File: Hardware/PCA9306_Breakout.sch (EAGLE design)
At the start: 15 parts

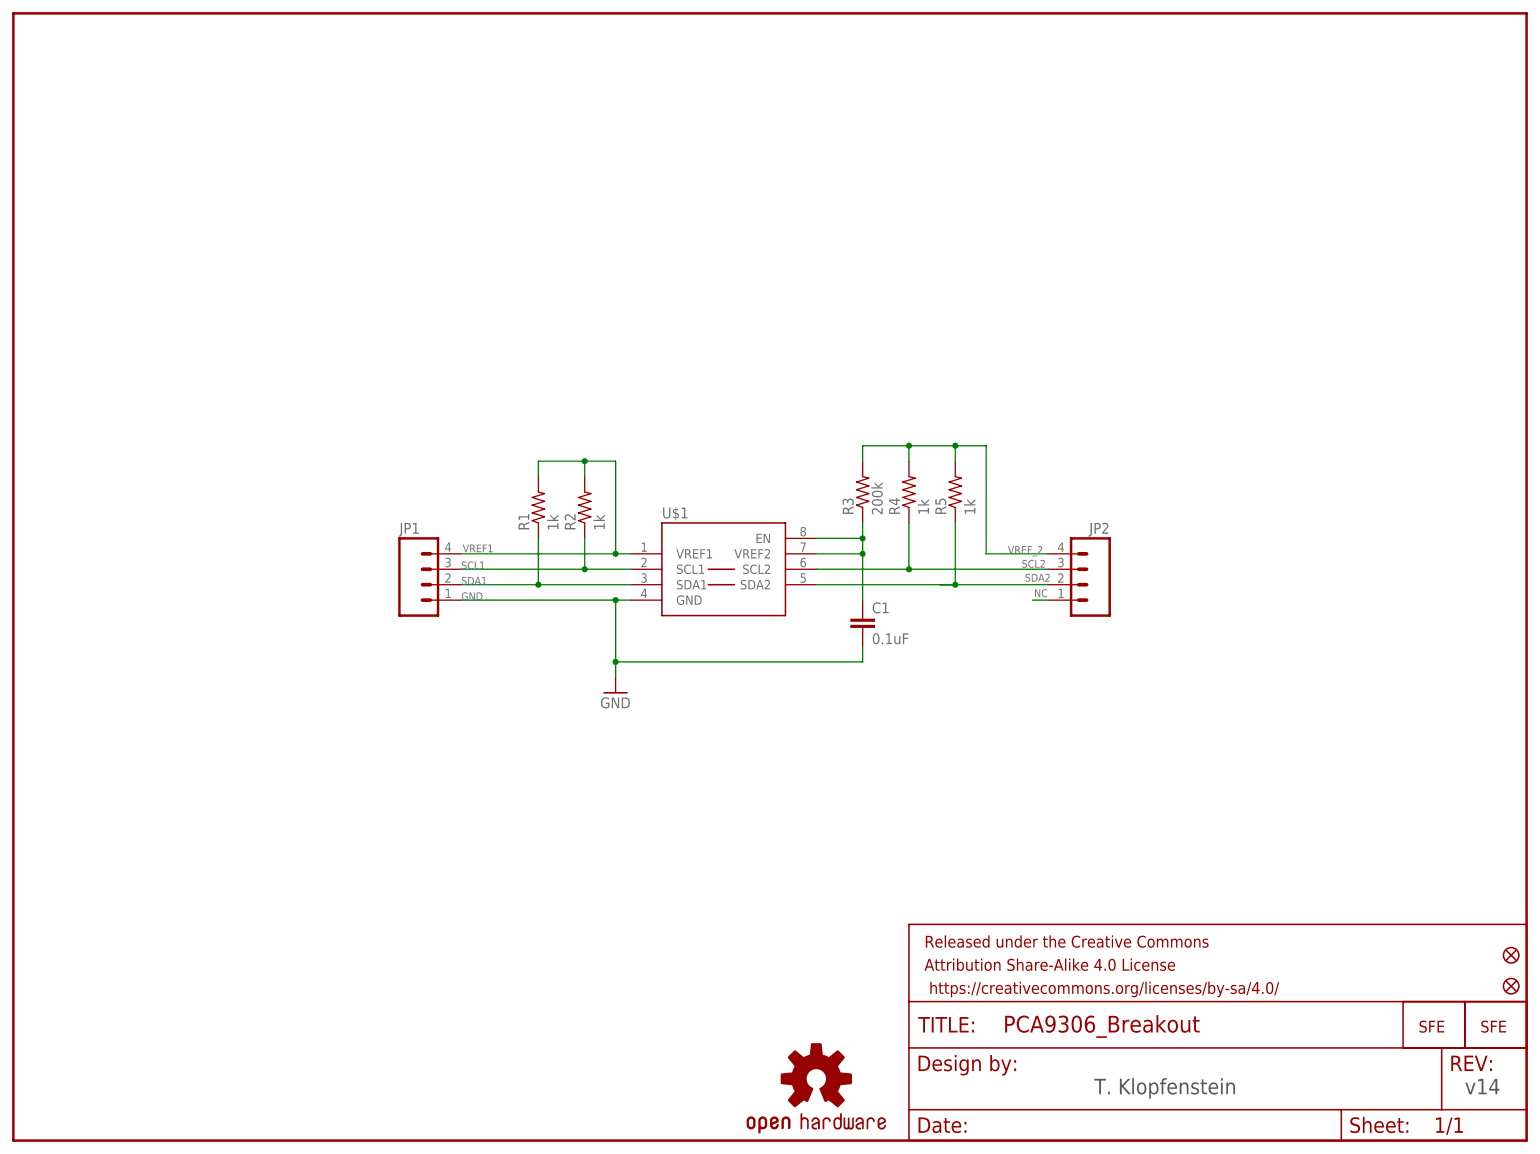
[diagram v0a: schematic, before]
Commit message: Adds slik lables, adds jumper for enable pin, increases size by 10 mils in both x and y direction, updates PCA9306 to new package
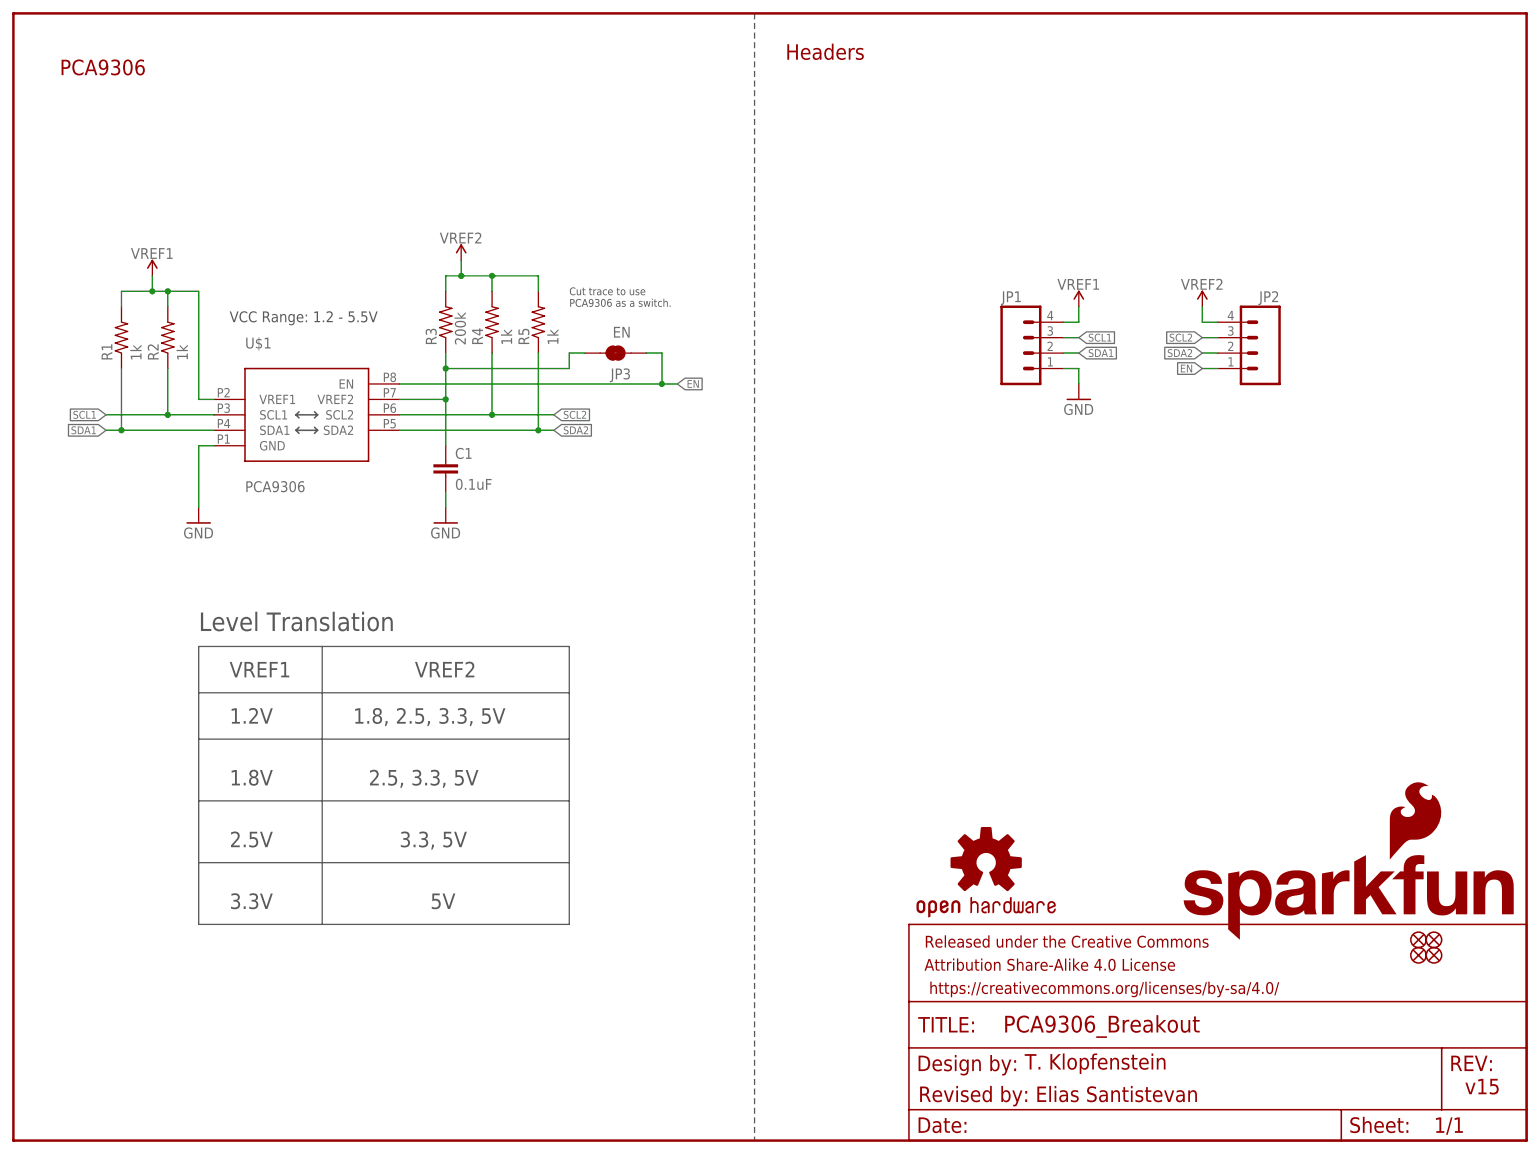
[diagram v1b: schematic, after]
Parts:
- removed JP4: LOGO-SFESK, SparkFun:LOGO-SFESK
- removed JP7, JP8: FIDUCIAL1X2.5, abes:FIDUCIAL1X2.5
- added FD1, FD2, FD3, FD4: FIDUCIALUFIDUCIAL, SparkFun-Aesthetics:FIDUCIALUFIDUCIAL
- added LOGO2: SFE_LOGO_FLAME.1_INCH, SparkFun-Aesthetics:SFE_LOGO_FLAME.1_INCH
- added LOGO3: SFE_LOGO_NAME.1_INCH, SparkFun-Aesthetics:SFE_LOGO_NAME.1_INCH
- C1: device SparkFun:CAP0603-CAP -> SparkFun-Capacitors:0.1UF-0603-25V-(+80/-20%)
- JP1, JP2: device SparkFun:M04PTH -> SparkFun-Connectors:CONN_041X04_NO_SILK
- JP3: value LOGO-SFESK -> EN; device SparkFun:LOGO-SFESK -> SparkFun-Jumpers:JUMPER-SMT_2_NC_TRACE_SILK
- R1, R2, R4, R5: device SparkFun:RESISTOR0603-RES -> SparkFun-Resistors:1KOHM-0603-1/10W-1%
- R3: device SparkFun:RESISTOR0603-RES -> SparkFun-Resistors:200KOHM-0603-1/10W-1%
- U$1: value (none) -> PCA9306; device SparkFun-DigitalIC:PCA9306 -> SparkFun-IC-Comms:PCA9306VSSOP_8PIN
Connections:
- removed net NC: JP2.1
- removed net VREF_2: JP2.4, R3.2, R4.2, R5.2
- new net EN: JP2.1, JP3.1, U$1.EN
- new net VREF2_IN: C1.1, JP3.2, R3.1, U$1.VREF2
- net VREF2: now also JP2.4, R3.2, R4.2, R5.2; no longer C1.1, R3.1, U$1.EN, U$1.VREF2
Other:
- note added: "1.2V"
- note added: "1.8, 2.5, 3.3, 5V"
- note added: "1.8V"
- note added: "2.5, 3.3, 5V"
- note added: "2.5V"
- note added: "3.3, 5V"
- note added: "3.3V"
- note added: "5V"
- note added: "Cut trace to use PCA9306 as a switch."
- note added: "Headers"
- note added: "Level Translation"
- note added: "PCA9306"
- note added: "Revised by: Elias Santistevan"
- note added: "VCC Range: 1.2 - 5.5V"
- note added: "VREF1"
- note added: "VREF2"
- note added: "v15"
- note removed: "v14"
- moved on the sheet: C1, R1, R2, R3, R4, R5

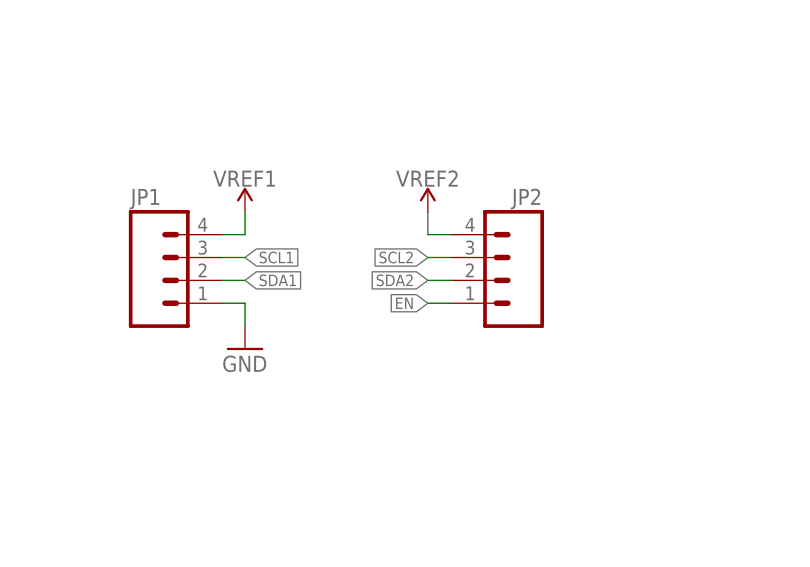
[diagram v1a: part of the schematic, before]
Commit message: Adds an additional PTH header for GND on VREF2 side
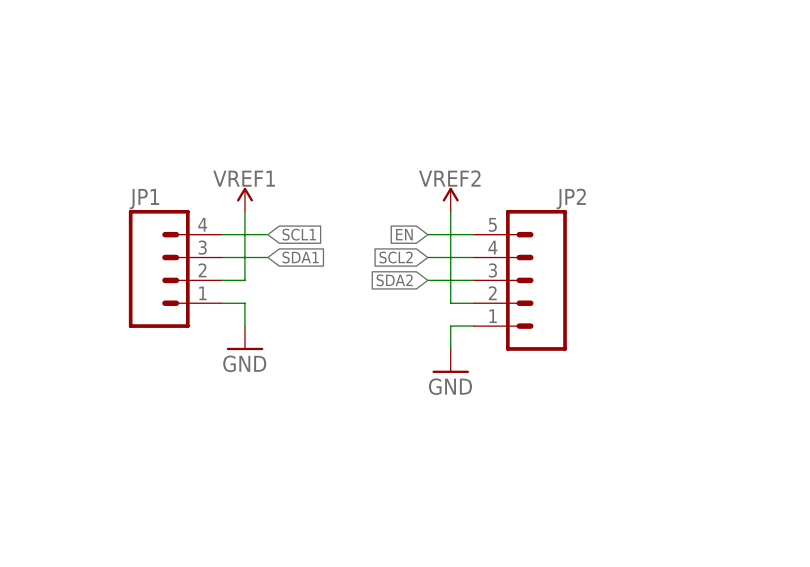
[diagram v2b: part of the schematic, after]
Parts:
- JP2: device SparkFun-Connectors:CONN_041X04_NO_SILK -> SparkFun-Connectors:CONN_05NO_SILK
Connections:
- net EN: now also JP2.5; no longer JP2.1
- net GND: now also JP2.1
- net SCL1: now also JP1.4; no longer JP1.3
- net SCL2: now also JP2.4; no longer JP2.3
- net SDA1: now also JP1.3; no longer JP1.2
- net SDA2: now also JP2.3; no longer JP2.2
- net VREF1: now also JP1.2; no longer JP1.4
- net VREF2: now also JP2.2; no longer JP2.4
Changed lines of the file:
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@@
 <part name="GND1" library="SparkFun-PowerSymbols" deviceset="GND" device=""/>
 <part name="JP1" library="SparkFun-Connectors" deviceset="CONN_04" device="1X04_NO_SILK"/>
-<part name="JP2" library="SparkFun-Connectors" deviceset="CONN_04" device="1X04_NO_SILK"/>
+<part name="JP2" library="SparkFun-Connectors" deviceset="CONN_05" device="NO_SILK"/>
 <part name="LOGO1" library="SparkFun-Aesthetics" deviceset="OSHW-LOGO" device="S"/>
 <part name="SUPPLY1" library="SparkFun-PowerSymbols" deviceset="VREF1" device=""/>
@@
 <part name="FD4" library="SparkFun-Aesthetics" deviceset="FIDUCIAL" device="UFIDUCIAL"/>
 <part name="LOGO3" library="SparkFun-Aesthetics" deviceset="SFE_LOGO_NAME" device=".1_INCH"/>
+<part name="GND4" library="SparkFun-PowerSymbols" deviceset="GND" device=""/>
 </parts>
 <sheets>
@@
 <attribute name="NAME" x="162.56" y="137.922" size="1.778" layer="95"/>
 </instance>
-<instance part="JP2" gate="J1" x="203.2" y="129.54" smashed="yes" rot="MR0">
-<attribute name="VALUE" x="208.28" y="121.92" size="1.778" layer="96" rot="MR0"/>
-<attribute name="NAME" x="208.28" y="137.922" size="1.778" layer="95" rot="MR0"/>
+<instance part="JP2" gate="G$1" x="208.28" y="129.54" smashed="yes" rot="MR0">
+<attribute name="VALUE" x="213.36" y="121.92" size="1.778" layer="96" rot="MR0"/>
+<attribute name="NAME" x="213.36" y="137.922" size="1.778" layer="95" rot="MR0"/>
 </instance>
 <instance part="LOGO1" gate="G$1" x="160.02" y="45.72" smashed="yes"/>
@@
 <attribute name="VALUE" x="175.26" y="139.954" size="1.778" layer="96" align="bottom-center"/>
 </instance>
-<instance part="SUPPLY4" gate="G$1" x="195.58" y="137.16" smashed="yes">
-<attribute name="VALUE" x="195.58" y="139.954" size="1.778" layer="96" align="bottom-center"/>
+<instance part="SUPPLY4" gate="G$1" x="198.12" y="137.16" smashed="yes">
+<attribute name="VALUE" x="198.12" y="139.954" size="1.778" layer="96" align="bottom-center"/>
 </instance>
 <instance part="JP3" gate="G$1" x="99.06" y="129.54" smashed="yes" rot="R180">
@@
 <instance part="FD4" gate="G$1" x="233.68" y="30.48" smashed="yes"/>
 <instance part="LOGO3" gate="G$1" x="190.5" y="33.02" smashed="yes"/>
+<instance part="GND4" gate="1" x="198.12" y="119.38" smashed="yes">
+<attribute name="VALUE" x="195.58" y="116.84" size="1.778" layer="96"/>
+</instance>
 </instances>
 <busses>
@@
 </segment>
 <segment>
-<pinref part="JP1" gate="J1" pin="3"/>
-<wire x1="172.72" y1="132.08" x2="175.26" y2="132.08" width="0.1524" layer="91"/>
-<label x="175.26" y="132.08" size="1.27" layer="95" font="vector" xref="yes"/>
+<pinref part="JP1" gate="J1" pin="4"/>
+<wire x1="172.72" y1="134.62" x2="177.8" y2="134.62" width="0.1524" layer="91"/>
+<label x="177.8" y="134.62" size="1.27" layer="95" xref="yes"/>
 </segment>
 </net>
@@
 </segment>
 <segment>
-<pinref part="JP1" gate="J1" pin="2"/>
-<wire x1="172.72" y1="129.54" x2="175.26" y2="129.54" width="0.1524" layer="91"/>
-<label x="175.26" y="129.54" size="1.27" layer="95" font="vector" xref="yes"/>
+<pinref part="JP1" gate="J1" pin="3"/>
+<wire x1="172.72" y1="132.08" x2="177.8" y2="132.08" width="0.1524" layer="91"/>
+<label x="177.8" y="132.08" size="1.27" layer="95" xref="yes"/>
 </segment>
 </net>
@@
 <pinref part="GND3" gate="1" pin="GND"/>
 <wire x1="175.26" y1="127" x2="175.26" y2="124.46" width="0.1524" layer="91"/>
+</segment>
+<segment>
+<pinref part="JP2" gate="G$1" pin="1"/>
+<wire x1="200.66" y1="124.46" x2="198.12" y2="124.46" width="0.1524" layer="91"/>
+<pinref part="GND4" gate="1" pin="GND"/>
+<wire x1="198.12" y1="121.92" x2="198.12" y2="124.46" width="0.1524" layer="91"/>
 </segment>
 </net>
@@
 </segment>
 <segment>
-<pinref part="JP2" gate="J1" pin="4"/>
-<wire x1="198.12" y1="134.62" x2="195.58" y2="134.62" width="0.1524" layer="91"/>
-<wire x1="195.58" y1="134.62" x2="195.58" y2="137.16" width="0.1524" layer="91"/>
+<pinref part="JP2" gate="G$1" pin="2"/>
+<wire x1="200.66" y1="127" x2="198.12" y2="127" width="0.1524" layer="91"/>
 <pinref part="SUPPLY4" gate="G$1" pin="VREF2"/>
+<wire x1="198.12" y1="127" x2="198.12" y2="137.16" width="0.1524" layer="91"/>
 </segment>
 </net>
@@
 </segment>
 <segment>
-<pinref part="JP2" gate="J1" pin="3"/>
-<wire x1="198.12" y1="132.08" x2="195.58" y2="132.08" width="0.1524" layer="91"/>
-<label x="195.58" y="132.08" size="1.27" layer="95" font="vector" rot="R180" xref="yes"/>
+<pinref part="JP2" gate="G$1" pin="4"/>
+<wire x1="200.66" y1="132.08" x2="195.58" y2="132.08" width="0.1524" layer="91"/>
+<label x="195.58" y="132.08" size="1.27" layer="95" rot="R180" xref="yes"/>
 </segment>
 </net>
@@
 </segment>
 <segment>
-<pinref part="JP2" gate="J1" pin="2"/>
-<wire x1="198.12" y1="129.54" x2="195.58" y2="129.54" width="0.1524" layer="91"/>
-<label x="195.58" y="129.54" size="1.27" layer="95" font="vector" rot="R180" xref="yes"/>
+<pinref part="JP2" gate="G$1" pin="3"/>
+<wire x1="200.66" y1="129.54" x2="195.58" y2="129.54" width="0.1524" layer="91"/>
+<label x="195.58" y="129.54" size="1.27" layer="95" rot="R180" xref="yes"/>
 </segment>
 </net>
@@
 </segment>
 <segment>
-<pinref part="JP1" gate="J1" pin="4"/>
-<wire x1="172.72" y1="134.62" x2="175.26" y2="134.62" width="0.1524" layer="91"/>
-<wire x1="175.26" y1="134.62" x2="175.26" y2="137.16" width="0.1524" layer="91"/>
+<pinref part="JP1" gate="J1" pin="2"/>
+<wire x1="172.72" y1="129.54" x2="175.26" y2="129.54" width="0.1524" layer="91"/>
 <pinref part="SUPPLY3" gate="G$1" pin="VREF1"/>
+<wire x1="175.26" y1="129.54" x2="175.26" y2="137.16" width="0.1524" layer="91"/>
 </segment>
 </net>
@@
 </segment>
 <segment>
-<pinref part="JP2" gate="J1" pin="1"/>
-<wire x1="198.12" y1="127" x2="195.58" y2="127" width="0.1524" layer="91"/>
-<label x="195.58" y="127" size="1.27" layer="95" font="vector" rot="R180" xref="yes"/>
-</segment>
-</net>
+<pinref part="JP2" gate="G$1" pin="5"/>
+<label x="195.58" y="134.62" size="1.27" layer="95" rot="R180" xref="yes"/>
+<wire x1="200.66" y1="134.62" x2="195.58" y2="134.62" width="0.1524" layer="91"/>
+</segment>
+</net>

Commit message: Moves passives to lower half of board, resulting in full retrace of board....
*Adds HIGH/LOW silk to board
*Adds triple jumper to correctly add enable feature
*Changes 0.1uF capacitor to 100pF capacitor
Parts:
- removed JP3: EN, SparkFun-Jumpers:JUMPER-SMT_2_NC_TRACE_SILK
- added JP4: EN, SparkFun-Jumpers:JUMPER-SMT_3_1-NC_TRACE_SILK
- C1: value 0.1uF -> 100pF; device SparkFun-Capacitors:0.1UF-0603-25V-(+80/-20%) -> SparkFun-Capacitors:100PF-0603-50V-5%
- LOGO1: value OSHW-LOGOS -> OSHW-LOGOMINI; device SparkFun-Aesthetics:OSHW-LOGOS -> SparkFun-Aesthetics:OSHW-LOGOMINI
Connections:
- new net JUMPER_IN: JP4.2, R3.2
- net EN: now also JP4.1; no longer JP3.1, U$1.EN
- net VREF2: now also JP4.3; no longer R3.2
- net VREF2_IN: now also U$1.EN; no longer JP3.2
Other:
- note added: "Logic Level Translator PCA9306"
- note added: "To enable enable, cut trace and fill in lower jumper."
- note removed: "Cut trace to use PCA9306 as a switch."
- note removed: "PCA9306"
- moved on the sheet: C1, R3, R4, R5

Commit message: Updates silk on jumper and "HIGH" and "LOW" voltages on bottom, renumbers parts in schematic
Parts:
- removed JP4: EN, SparkFun-Jumpers:JUMPER-SMT_3_1-NC_TRACE_SILK
- added J1: (no value), SparkFun-Connectors:CONN_041X04_NO_SILK
- JP1: value (none) -> EN; device SparkFun-Connectors:CONN_041X04_NO_SILK -> SparkFun-Jumpers:JUMPER-SMT_3_1-NC_TRACE_SILK
- LOGO2: value SFE_LOGO_FLAME.1_INCH -> SFE_LOGO_NAME.1_INCH; device SparkFun-Aesthetics:SFE_LOGO_FLAME.1_INCH -> SparkFun-Aesthetics:SFE_LOGO_NAME.1_INCH
- LOGO3: value SFE_LOGO_NAME.1_INCH -> SFE_LOGO_FLAME.1_INCH; device SparkFun-Aesthetics:SFE_LOGO_NAME.1_INCH -> SparkFun-Aesthetics:SFE_LOGO_FLAME.1_INCH
- R1, R2, R4, R5: value 1k -> 2.2k; device SparkFun-Resistors:1KOHM-0603-1/10W-1% -> SparkFun-Resistors:2.2KOHM-0603-1/10W-1%
- renumbered JP2 to J2, U$1 to U1
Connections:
- net EN: now also JP1.1; no longer JP4.1
- net GND: now also J1.1; no longer JP1.1
- net JUMPER_IN: now also JP1.2; no longer JP4.2
- net SCL1: now also J1.4; no longer JP1.4
- net SDA1: now also J1.3; no longer JP1.3
- net VREF1: now also J1.2; no longer JP1.2
- net VREF2: now also JP1.3; no longer JP4.3

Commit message: Fixes traces for both data lines, corrects punctuation of schematic note.
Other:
- note added: "To enable, enable: cut trace and fill in lower jumper."
- note removed: "To enable enable, cut trace and fill in lower jumper."
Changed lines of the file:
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@@
 <text x="68.58" y="38.1" size="2.54" layer="97" font="vector">5V</text>
 <text x="33.02" y="137.16" size="1.778" layer="97" font="vector">VCC Range: 1.2 - 5.5V</text>
-<text x="83.82" y="152.4" size="1.27" layer="97" font="vector">To enable enable, cut trace
+<text x="83.82" y="152.4" size="1.27" layer="97" font="vector">To enable, enable: cut trace
 and fill in lower jumper.</text>
 <wire x1="83.82" y1="139.7" x2="93.98" y2="139.7" width="0.1524" layer="97" style="dashdot"/>
